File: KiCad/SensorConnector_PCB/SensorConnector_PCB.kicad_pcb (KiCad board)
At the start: 2 copper layers, 38 x 28 mm, 9 parts, among them J101 Conn_01x03, J102 Conn_01x03, J103 Conn_01x03, J104 Conn_01x03, J105 Conn_01x06

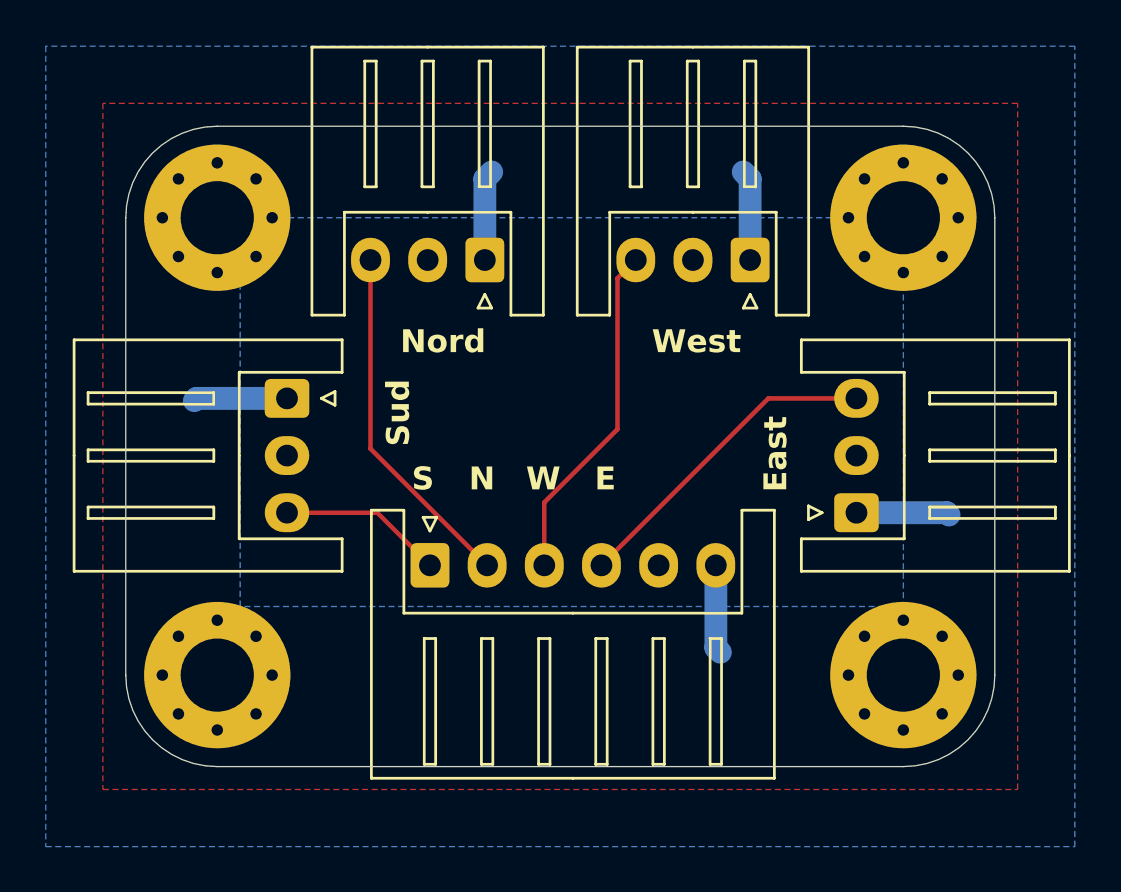
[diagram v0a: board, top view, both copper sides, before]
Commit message: update pcb connector files
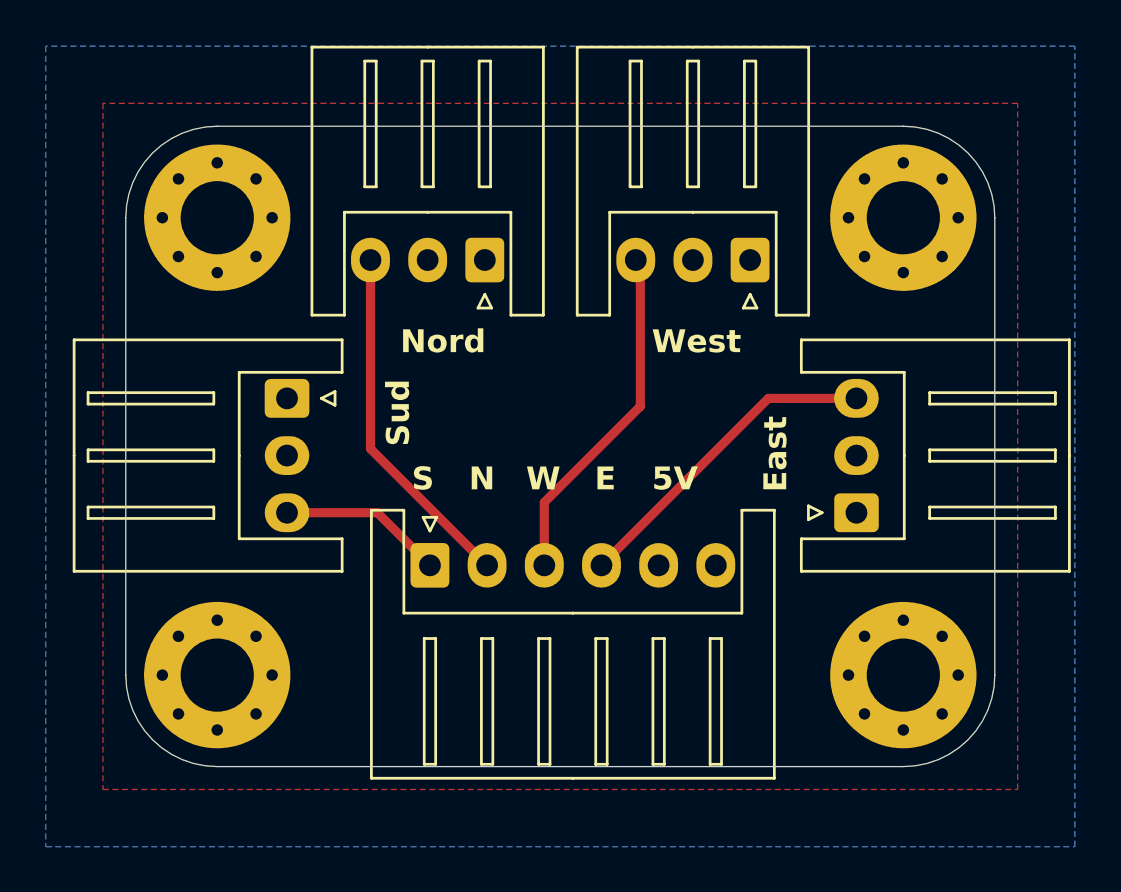
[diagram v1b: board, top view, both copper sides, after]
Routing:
- net GND: track 20.0 -> 0.00 mm
- added copper zone on F.Cu, net +5V
- removed copper zone on B.Cu, net +5V
- removed copper zone on F.Cu, net GND
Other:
- board text added: "5V"
- board text added: "Distance Sensor Adaptator TagBot L. CHAPART 22/10/2024"
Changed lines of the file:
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@@
 		(layer "Edge.Cuts")
+	)
+	(gr_text "Distance Sensor\nAdaptator TagBot\nL. CHAPART\n22/10/2024"
+		(at 124.5 83.5 0)
+		(layer "B.SilkS")
+		(effects
+			(font
+				(size 1.5 1.5)
+				(thickness 0.3)
+				(bold yes)
+			)
+			(justify left bottom mirror)
+		)
 	)
 	(gr_text "S"
@@
 		)
 	)
+	(gr_text "5V"
+		(at 119 82 0)
+		(layer "F.SilkS")
+		(effects
+			(font
+				(size 1 1)
+				(thickness 0.2)
+				(bold yes)
+			)
+			(justify left bottom)
+		)
+	)
 	(gr_text "Nord"
 		(at 108 76 0)
@@
 	)
 	(segment
-		(start 123.3 71.85)
-		(end 123.3 68.3)
-		(width 1)
-		(layer "B.Cu")
-		(net 2)
-	)
-	(segment
-		(start 111.7 71.85)
-		(end 111.7 68.3)
-		(width 1)
-		(layer "B.Cu")
-		(net 2)
-	)
-	(segment
-		(start 132 83)
-		(end 131.9 82.9)
-		(width 1)
-		(layer "B.Cu")
-		(net 2)
-	)
-	(segment
-		(start 123.3 68.3)
-		(end 123 68)
-		(width 1)
-		(layer "B.Cu")
-		(net 2)
-	)
-	(segment
-		(start 127.95 82.9)
-		(end 131.9 82.9)
-		(width 1)
-		(layer "B.Cu")
-		(net 2)
-	)
-	(segment
-		(start 103.05 77.9)
-		(end 99.1 77.9)
-		(width 1)
-		(layer "B.Cu")
-		(net 2)
-	)
-	(segment
-		(start 112 68)
-		(end 111.7 68.3)
-		(width 1)
-		(layer "B.Cu")
-		(net 2)
-	)
-	(segment
-		(start 121.8 85.2)
-		(end 121.8 88.8)
-		(width 1)
-		(layer "B.Cu")
-		(net 2)
-	)
-	(segment
-		(start 122 89)
-		(end 121.8 88.8)
-		(width 1)
-		(layer "B.Cu")
-		(net 2)
-	)
-	(segment
-		(start 99.1 77.9)
-		(end 99 78)
-		(width 1)
-		(layer "B.Cu")
-		(net 2)
-	)
-	(segment
 		(start 106.7 80.1)
 		(end 111.8 85.2)
-		(width 0.2)
+		(width 0.4)
 		(layer "F.Cu")
 		(net 3)
@@
 		(start 106.7 71.85)
 		(end 106.7 80.1)
-		(width 0.2)
+		(width 0.4)
 		(layer "F.Cu")
 		(net 3)
 	)
 	(segment
-		(start 117.5 72.65)
-		(end 117.5 79.25)
-		(width 0.2)
-		(layer "F.Cu")
-		(net 4)
-	)
-	(segment
-		(start 117.5 79.25)
+		(start 118.3 71.85)
+		(end 118.5 72.05)
+		(width 0.4)
+		(layer "F.Cu")
+		(net 4)
+	)
+	(segment
+		(start 118.5 78.25)
 		(end 114.3 82.45)
-		(width 0.2)
-		(layer "F.Cu")
-		(net 4)
-	)
-	(segment
-		(start 118.3 71.85)
-		(end 117.5 72.65)
-		(width 0.2)
+		(width 0.4)
 		(layer "F.Cu")
 		(net 4)
@@
 		(start 114.3 82.45)
 		(end 114.3 85.2)
-		(width 0.2)
+		(width 0.4)
+		(layer "F.Cu")
+		(net 4)
+	)
+	(segment
+		(start 118.5 72.05)
+		(end 118.5 78.25)
+		(width 0.4)
 		(layer "F.Cu")
 		(net 4)
@@
 		(start 103.05 82.9)
 		(end 107 82.9)
-		(width 0.2)
+		(width 0.4)
 		(layer "F.Cu")
 		(net 5)
@@
 		(start 107 82.9)
 		(end 109.3 85.2)
-		(width 0.2)
+		(width 0.4)
 		(layer "F.Cu")
 		(net 5)
@@
 		(start 127.95 77.9)
 		(end 124.1 77.9)
-		(width 0.2)
+		(width 0.4)
 		(layer "F.Cu")
 		(net 6)
@@
 		(start 124.1 77.9)
 		(end 116.8 85.2)
-		(width 0.2)
+		(width 0.4)
 		(layer "F.Cu")
 		(net 6)
 	)
 	(zone
-		(net 2)
-		(net_name "GND")
+		(net 1)
+		(net_name "+5V")
 		(layer "F.Cu")
 		(hatch edge 0.5)
-		(connect_pads
+		(connect_pads yes
 			(clearance 0.5)
 		)
@@
 			(pts
 				(xy 95 65) (xy 95 95) (xy 135 95) (xy 135 65)
-			)
-		)
-	)
-	(zone
-		(net 1)
-		(net_name "+5V")
-		(layer "B.Cu")
-		(hatch edge 0.5)
-		(priority 2)
-		(connect_pads
-			(clearance 0.5)
-		)
-		(min_thickness 0.25)
-		(filled_areas_thickness no)
-		(fill yes
-			(thermal_gap 0.5)
-			(thermal_bridge_width 0.5)
-		)
-		(polygon
-			(pts
-				(xy 101 70) (xy 130 70) (xy 130 87) (xy 101 87)
 			)
 		)
@@
 		(hatch edge 0.5)
 		(priority 1)
-		(connect_pads
+		(connect_pads yes
 			(clearance 0.5)
 		)
